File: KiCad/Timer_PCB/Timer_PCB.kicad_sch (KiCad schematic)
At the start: 22 parts, among them J1 JST_05, SW1 SW_SPDT, SW2 SW_SPDT, SW3 SW_SPDT, SW4 SW_SPDT, U1 ULN2003, U3 ULN2003, U4 ULN2003

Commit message: avancement kicad
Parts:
- added C2, C3: 10uF, symbol Device:C
- added J2, J3: JST_05, Connector_JST:JST_EH_B5B-EH-A_1x05_P2.50mm_Vertical, symbol PCM_SL_Connectors:JST_05
- U3, U4: footprint (none) -> Package_SO:SOIC-16_4.55x10.3mm_P1.27mm; LCSC (none) -> C7512
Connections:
- net +5V: now also U3.9 (COM), U4.9 (COM), C2.1, C3.1, J2.1, J3.1
- net GND: now also C2.2, C3.2; no longer BT1.1 (+), D1.5 (VDD), D2.5 (VDD), D3.5 (VDD), D4.5 (VDD), D5.5 (VDD), D6.5 (VDD), D7.5 (VDD), D8.5 (VDD), D9.5 (VDD), U2.15 (3V), condensateur1.1, condensateur2.1
- net M1A: now also U3.1 (I1), U4.1 (I1)
- net M1B: now also U3.2 (I2), U4.2 (I2)
- net M1C: now also U3.3 (I3), U4.3 (I3)
- net M1D: now also U3.4 (I4), U4.4 (I4)
- net at U3.13 (O4): now also J2.5
- net at U3.14 (O3): now also J2.4
- net at U3.15 (O2): now also J2.3
- net at U3.16 (O1): now also J2.2
- net at U4.13 (O4): now also J3.5
- net at U4.14 (O3): now also J3.4
- net at U4.15 (O2): now also J3.3
- net at U4.16 (O1): now also J3.2
- new net: BT1.1 (+), D1.5 (VDD), D2.5 (VDD), D3.5 (VDD), D4.5 (VDD), D5.5 (VDD), D6.5 (VDD), D7.5 (VDD), D8.5 (VDD), D9.5 (VDD), U2.15 (3V), condensateur1.1, condensateur2.1
- no-connect marks 7 -> 19

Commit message: avancement de l'article sur l'utilisation de Kicad
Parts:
- removed D1, D2, D3, D4, D5, D6, D7, D8, D9: WS2812, LED_SMD:LED_WS2812_PLCC6_5.0x5.0mm_P1.6mm, symbol LED:WS2812
- removed SW1, SW2, SW3, SW4: SW_SPDT, symbol Switch:SW_SPDT
- added D10, D11, D12, D13, D14, D15, D16, D17, D18: WS2812, LED_SMD:LED_WS2812_PLCC6_5.0x5.0mm_P1.6mm, symbol LED:WS2812
- added SW5: SW_SPDT_Switch_Led_Control, symbol Switch:SW_SPDT
- added SW6: SW_SPDT_Switch_Motor_1, symbol Switch:SW_SPDT
- added SW7: SW_SPDT_Switch_Motor_2, symbol Switch:SW_SPDT
- added SW8: SW_SPDT_Switch_Motor_3, symbol Switch:SW_SPDT
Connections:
- net +5V: now also D10.5 (VDD), D11.5 (VDD), D12.5 (VDD), D13.5 (VDD), D14.5 (VDD), D15.5 (VDD), D16.5 (VDD), D17.5 (VDD), D18.5 (VDD)
- net GND: now also D10.6 (VSS), D11.6 (VSS), D12.6 (VSS), D13.6 (VSS), D14.6 (VSS), D15.6 (VSS), D16.6 (VSS), D17.6 (VSS), D18.6 (VSS), SW5.2 (B), SW6.2 (B), SW7.2 (B), SW8.2 (B); no longer BT1.2 (-), U2.21 (GPIO38), U2.25 (GPIO21), U2.26 (GPIO18), U2.27 (GPIO17), U2.29 (GND), U2.30 (GND), condensateur1.2, condensateur2.2
- net M1A: no longer U3.1 (I1), U4.1 (I1)
- net M1B: no longer U3.2 (I2), U4.2 (I2)
- net M1C: no longer U3.3 (I3), U4.3 (I3)
- net M1D: no longer U3.4 (I4), U4.4 (I4)
- net M2C: now reaches U2.10 (GPIO7)
- net M2C: now also U3.3 (I3)
- net M2D: now reaches U2.11 (GPIO11)
- net M2D: now also U3.4 (I4)
- net M3A: now reaches U2.12 (GPIO8)
- net M3A: now also U4.1 (I1)
- net M3B: now reaches U2.13 (GPIO10)
- net M3B: now also U4.2 (I2)
- net M3C: now reaches U2.14 (GPIO9)
- net M3C: now also U4.3 (I3)
- net at BT1.1 (+), U2.15 (3V): no longer condensateur1.1, condensateur2.1
- net M3D: now reaches U2.16 (GPIO14)
- net M3D: now also U4.4 (I4)
- net WS2812_Led: now reaches U2.17 (GPIO33)
- net Switch_motor_3_Down: now reaches U2.22 (GPIO36)
- net Switch_motor_2_Up: now reaches U2.23 (GPIO34)
- net Switch_motor_2_Down: now reaches U2.24 (GPIO35)
- net Switch_Led_control_Down: now reaches U2.28 (GPIO16)
- net at U2.31 (GPIO15): now also condensateur1.1, condensateur2.1
- net M2A: now reaches U2.8 (GPIO6)
- net M2A: now also U3.1 (I1)
- net M2B: now reaches U2.9 (GPIO13)
- net M2B: now also U3.2 (I2)
- new net: D14.1 (DOUT), D17.2 (DIN)
- new net: D14.2 (DIN), D16.1 (DOUT)
- new net: D15.1 (DOUT), D16.2 (DIN)
- new net: D13.1 (DOUT), D15.2 (DIN)
- new net: D17.1 (DOUT), D18.2 (DIN)
- new net: BT1.2 (-), condensateur1.2, condensateur2.2
- new net: D12.1 (DOUT), D13.2 (DIN)
- new net: D11.1 (DOUT), D12.2 (DIN)
- new net: D10.1 (DOUT), D11.2 (DIN)
- new net GPIO16: SW5.1 (A)
- new net GPIO17: SW5.3 (C)
- new net GPIO18: SW6.1 (A)
- new net GPIO21: SW6.3 (C)
- new net GPIO33: D10.2 (DIN)
- new net GPIO34: SW7.1 (A)
- new net GPIO35: SW7.3 (C)
- new net GPIO36: SW8.3 (C)
- new net GPIO38: SW8.1 (A)
- new net Switch_Led_control_Up: U2.27 (GPIO17)
- new net Switch_motor_1_Down: U2.26 (GPIO18)
- new net Switch_motor_1_Up: U2.25 (GPIO21)
- new net Switch_motor_3_Up: U2.21 (GPIO38)
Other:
- note added: "ESP32"
- note added: "LED"
- note added: "Motor Driver"
- note added: "Switches"
- title: (none) -> Timer PCB
- moved on the sheet: BT1, C1, C2, C3, J1, J2, J3, U1, U2, U3, U4, condensateur1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

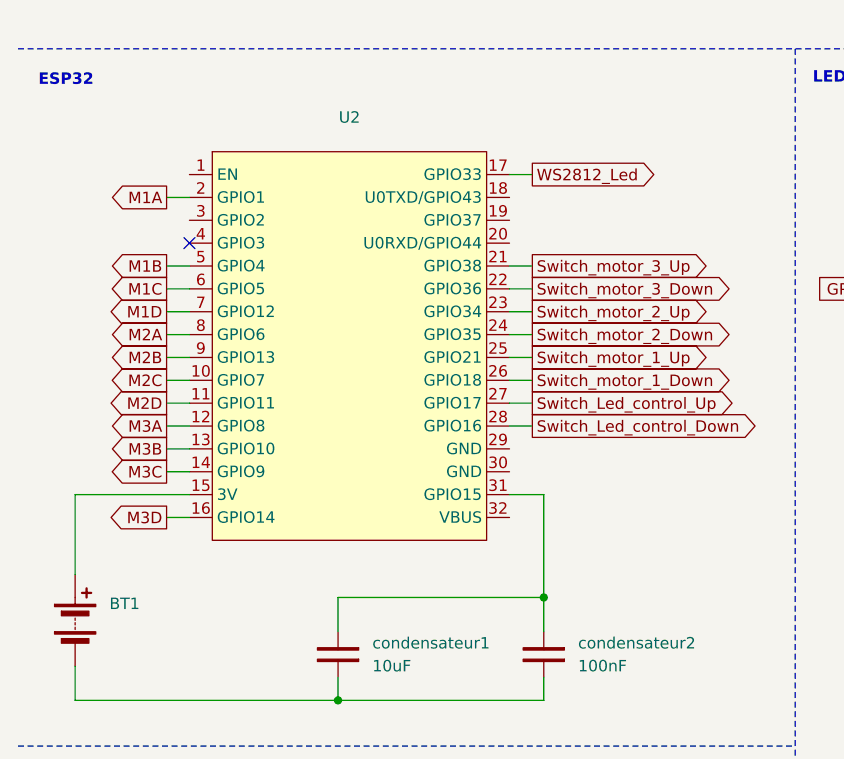
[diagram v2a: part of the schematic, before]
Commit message: dévellopement de l'article Kicad. Comment parametrer nbr couches PCB et créer zone connecté GND
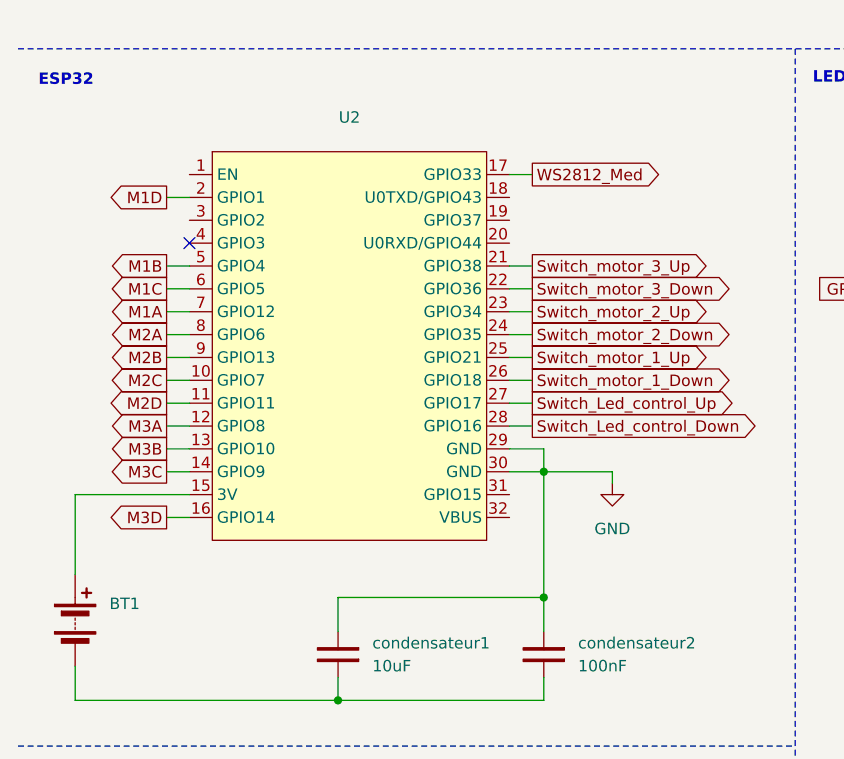
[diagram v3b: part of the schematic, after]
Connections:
- net GND: now also U2.29 (GND), U2.30 (GND), condensateur1.1, condensateur2.1
- net M1A: now also U2.7 (GPIO12); no longer U2.2 (GPIO1)
- net M1D: now also U2.2 (GPIO1); no longer U2.7 (GPIO12)
- net WS2812_Led renamed WS2812_Med
- now unconnected: U2.31 (GPIO15)
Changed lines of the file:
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@@
+	)
+	(junction
+		(at 69.85 123.19)
+		(diameter 0)
+		(color 0 0 0 0)
 	)
 	(junction
@@
 	(wire
 		(pts
+			(xy 27.94 100.33) (xy 30.48 100.33)
+		)
+		(stroke
+			(width 0)
+			(type default)
+		)
+	)
+	(wire
+		(pts
 			(xy 160.02 110.49) (xy 160.02 111.76)
 		)
@@
 	(wire
 		(pts
+			(xy 66.04 120.65) (xy 69.85 120.65)
+		)
+		(stroke
+			(width 0)
+			(type default)
+		)
+	)
+	(wire
+		(pts
 			(xy 182.88 43.18) (xy 177.8 43.18)
 		)
@@
 	(wire
 		(pts
+			(xy 27.94 92.71) (xy 30.48 92.71)
+		)
+		(stroke
+			(width 0)
+			(type default)
+		)
+	)
+	(wire
+		(pts
 			(xy 46.99 146.05) (xy 46.99 148.59)
 		)
@@
 	(wire
 		(pts
-			(xy 27.94 92.71) (xy 30.48 92.71)
+			(xy 77.47 123.19) (xy 77.47 124.46)
 		)
 		(stroke
@@
 	(wire
 		(pts
+			(xy 27.94 102.87) (xy 30.48 102.87)
+		)
+		(stroke
+			(width 0)
+			(type default)
+		)
+	)
+	(wire
+		(pts
 			(xy 139.7 147.32) (xy 139.7 148.59)
 		)
@@
 	(wire
 		(pts
+			(xy 69.85 120.65) (xy 69.85 123.19)
+		)
+		(stroke
+			(width 0)
+			(type default)
+		)
+	)
+	(wire
+		(pts
 			(xy 147.32 102.87) (xy 152.4 102.87)
 		)
@@
 	(wire
 		(pts
-			(xy 27.94 102.87) (xy 30.48 102.87)
+			(xy 69.85 123.19) (xy 77.47 123.19)
 		)
 		(stroke
@@
 	(wire
 		(pts
-			(xy 27.94 100.33) (xy 30.48 100.33)
-		)
-		(stroke
-			(width 0)
-			(type default)
-		)
-	)
-	(wire
-		(pts
 			(xy 73.66 187.96) (xy 76.2 187.96)
 		)
@@
 	(wire
 		(pts
+			(xy 27.94 105.41) (xy 30.48 105.41)
+		)
+		(stroke
+			(width 0)
+			(type default)
+		)
+	)
+	(wire
+		(pts
 			(xy 128.27 176.53) (xy 133.35 176.53)
 		)
@@
 	(wire
 		(pts
-			(xy 27.94 105.41) (xy 30.48 105.41)
-		)
-		(stroke
-			(width 0)
-			(type default)
-		)
-	)
-	(wire
-		(pts
 			(xy 91.44 40.64) (xy 93.98 40.64)
 		)
@@
 	(wire
 		(pts
-			(xy 69.85 125.73) (xy 69.85 137.16)
+			(xy 69.85 123.19) (xy 69.85 137.16)
 		)
 		(stroke
@@
 	(wire
 		(pts
+			(xy 66.04 123.19) (xy 69.85 123.19)
+		)
+		(stroke
+			(width 0)
+			(type default)
+		)
+	)
+	(wire
+		(pts
 			(xy 119.38 147.32) (xy 119.38 148.59)
-		)
-		(stroke
-			(width 0)
-			(type default)
-		)
-	)
-	(wire
-		(pts
-			(xy 66.04 125.73) (xy 69.85 125.73)
 		)
 		(stroke
@@
 		)
 	)
-	(global_label "WS2812_Led"
+	(global_label "WS2812_Med"
 		(shape output)
 		(at 68.58 90.17 0)
@@
 	(global_label "M1D"
 		(shape output)
-		(at 27.94 105.41 180)
-		(fields_autoplaced yes)
-		(effects
-			(font
-				(size 1.27 1.27)
-			)
-			(justify right)
-		)
-		(property "Intersheetrefs" "${INTERSHEET_REFS}"
-			(at 21.0239 105.41 0)
+		(at 27.94 92.71 180)
+		(fields_autoplaced yes)
+		(effects
+			(font
+				(size 1.27 1.27)
+			)
+			(justify right)
+		)
+		(property "Intersheetrefs" "${INTERSHEET_REFS}"
+			(at 21.0239 92.71 0)
 			(effects
 				(font
@@
 	(global_label "M1A"
 		(shape output)
-		(at 27.94 92.71 180)
-		(fields_autoplaced yes)
-		(effects
-			(font
-				(size 1.27 1.27)
-			)
-			(justify right)
-		)
-		(property "Intersheetrefs" "${INTERSHEET_REFS}"
-			(at 21.2053 92.71 0)
+		(at 27.94 105.41 180)
+		(fields_autoplaced yes)
+		(effects
+			(font
+				(size 1.27 1.27)
+			)
+			(justify right)
+		)
+		(property "Intersheetrefs" "${INTERSHEET_REFS}"
+			(at 21.2053 105.41 0)
 			(effects
 				(font
@@
 					(unit 1)
 				)
+			)
+		)
+	)
+	(symbol
+		(lib_id "power:GND")
+		(at 77.47 124.46 0)
+		(unit 1)
+		(exclude_from_sim no)
+		(in_bom yes)
+		(on_board yes)
+		(dnp no)
+		(fields_autoplaced yes)
+		(property "Reference" "#PWR034"
+			(at 77.47 130.81 0)
+			(effects
+				(font
+					(size 1.27 1.27)
+				)
+				(hide yes)
+			)
+		)
+		(property "Value" "GND"
+			(at 77.47 129.54 0)
+			(effects
+				(font
+					(size 1.27 1.27)
+				)
+			)
+		)
+		(property "Footprint" ""
+			(at 77.47 124.46 0)
+			(effects
+				(font
+					(size 1.27 1.27)
+				)
+				(hide yes)
+			)
+		)
+		(property "Datasheet" ""
+			(at 77.47 124.46 0)
+			(effects
+				(font
+					(size 1.27 1.27)
+				)
+				(hide yes)
+			)
+		)
+		(property "Description" "Power symbol creates a global label with name \"GND\" , ground"
+			(at 77.47 124.46 0)
+			(effects
+				(font
+					(size 1.27 1.27)
+				)
+				(hide yes)
+			)
+		)
+		(pin "1"
+		)
+		(instances
+			(project "Timer_PCB"
+				(path "/c4cfdf40-c3b2-4c58-998c-a7d7b70b9691"
+					(reference "#PWR034")
+					(unit 1)
+				)
